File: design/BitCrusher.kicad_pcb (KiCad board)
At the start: 2 copper layers, 181.5 x 86.2 mm, 135 parts, among them J1 BNC, J10 PJ-002BH, J2 BWSMA-KWE-Z001, J3 BWSMA-KE-Z001, J4 BWSMA-KE-Z001, J5 SHOU HAN TYPE-C 14P CC-2.6, J6 Conn_01x04_Pin, J7 Conn_01x04_Pin, J8 Conn_01x03_Pin, J9 Conn_01x03_Pin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

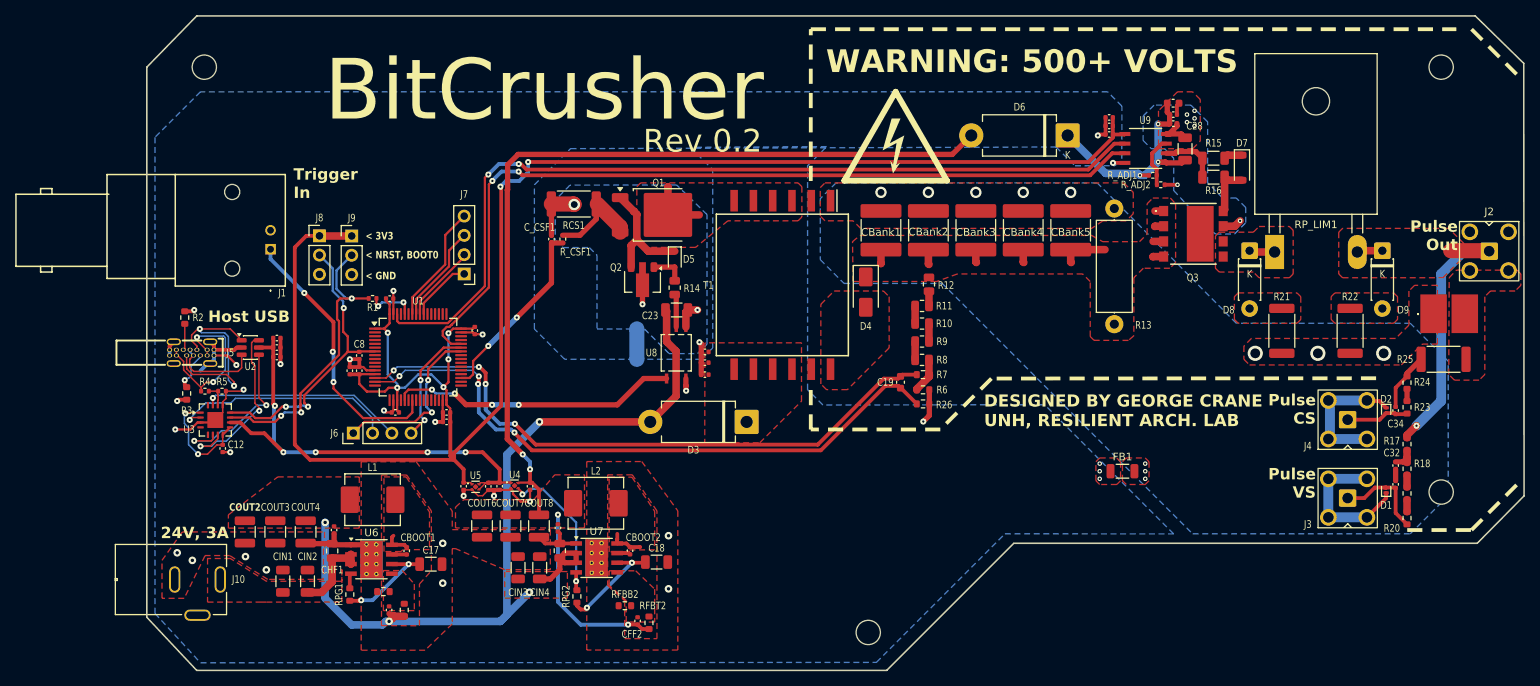
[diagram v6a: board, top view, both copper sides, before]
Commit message: Improved decoupling
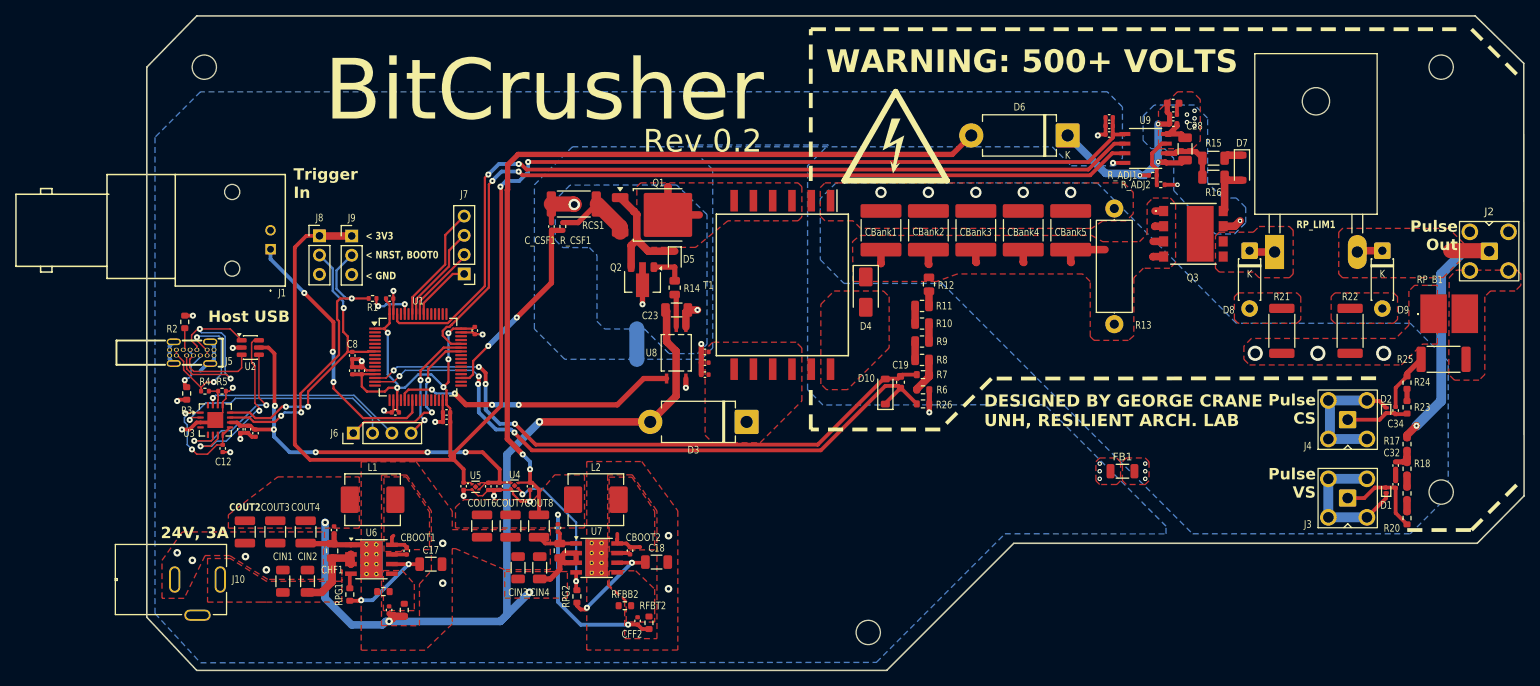
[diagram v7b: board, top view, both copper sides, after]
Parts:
- added D10: BZT52C3V3, Diode_SMD:D_SOD-123, F.Cu at (156.2, 103.2)
- R14: value 10 -> 22
- R15: value 2.2 0.75W -> 10 0.75W
- moved C9 13.0 mm to (71.2, 108.2), turned to -90 degrees
- moved C10 11.4 mm to (72.2, 108.2), turned to -90 degrees
- moved C11 10.4 mm to (73.2, 108.7), turned to -90 degrees
- moved C_CSF1 1.66 mm to (112.2, 81.5)
- moved R_CSF1 1.66 mm to (113.7, 81.5)
- moved C8 0.92 mm to (86.0, 98.5)
- moved R2 0.58 mm to (63.9, 94.1)
- moved L2 0.47 mm to (118.1, 117.5)
- moved C6 0.33 mm to (87.2, 100.5)
- moved C7 0.33 mm to (86.0, 100.5)
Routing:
- net GND: track 94.5 -> 84.8 mm
- net +5V: track 63.3 -> 58.7 mm
- net HVVS-: track 83.8 -> 86.8 mm
- net Net-(J5-D--PadA7): track 30.2 -> 27.6 mm
- net GNDFLY: track 20.0 -> 18.0 mm
- net Net-(Q1-S): track 12.4 -> 10.6 mm
- net HVCS: track 24.9 -> 26.5 mm
- net /Control & Interface/VBUS: track 22.2 -> 21.5 mm
- net Net-(J5-CC1): track 3.51 -> 2.93 mm
- net RST: track 39.1 -> 38.6 mm
- net +3V3: track 244.5 -> 244.0 mm

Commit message: Rev 0.2 Production
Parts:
- moved R_ADJ2 1.56 mm to (193.5, 74.8)
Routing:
- net Net-(U3-USBDP): track 21.6 -> 20.1 mm
- net Net-(U3-USBDM): track 23.4 -> 22.1 mm
- net Net-(U3-3V3OUT): track 15.0 -> 14.0 mm
- net TX_IN: track 30.1 -> 29.2 mm
- net GND: track 84.8 -> 83.9 mm, vias 30 -> 32
- net GND_DRV: track 10.7 -> 11.0 mm, vias 7 -> 11
- net PulseCS-: vias 11 -> 29
